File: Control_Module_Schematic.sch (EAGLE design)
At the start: 29 parts, among them U2 ATMEGA328P_TQFP

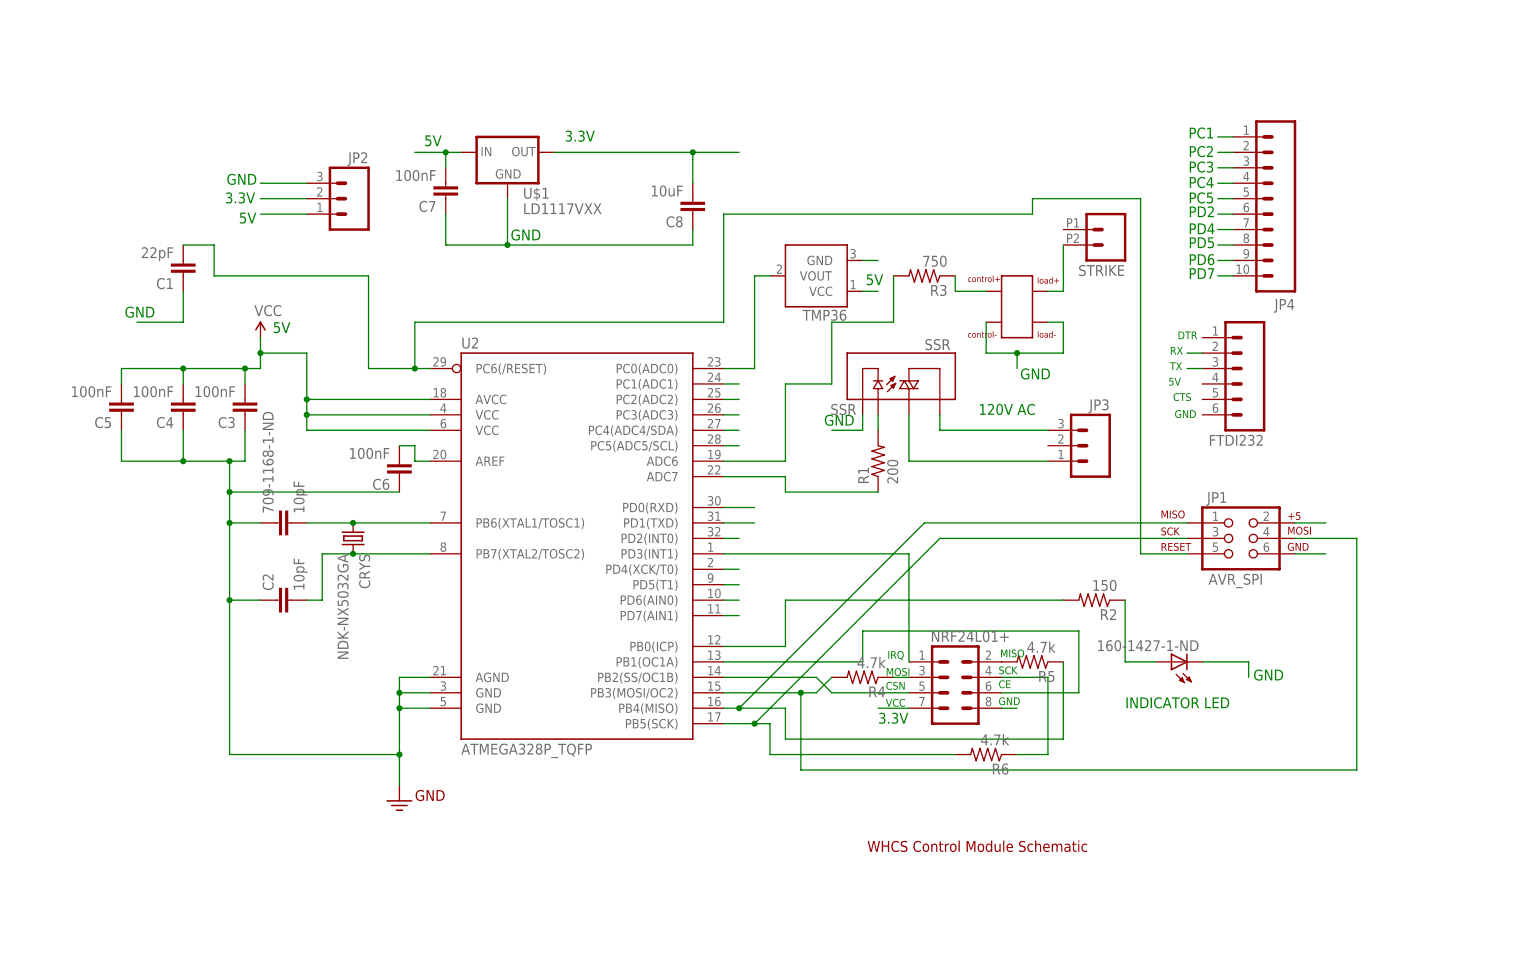
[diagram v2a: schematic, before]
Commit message: fixed drc fail. Two vias were too close together at the top right of the mcu
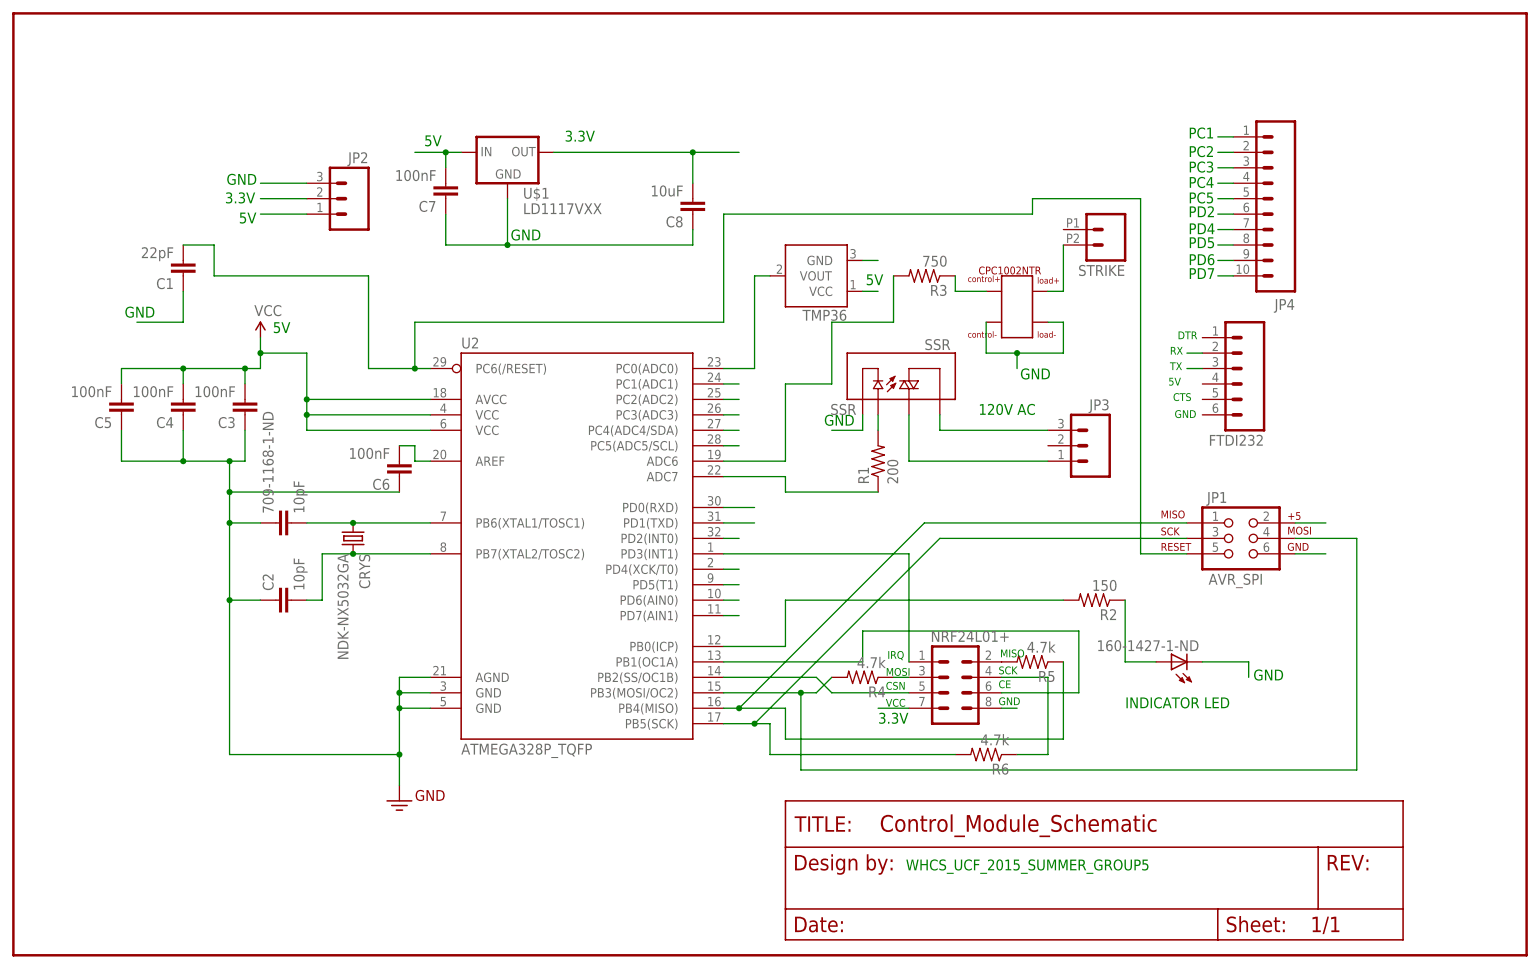
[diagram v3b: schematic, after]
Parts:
- added FRAME1: FRAME-LETTERNO_PACKAGE, WHCS:FRAME-LETTERNO_PACKAGE
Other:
- note added: "WHCS_UCF_2015_SUMMER_GROUP5"
- note removed: "WHCS Control Module Schematic"
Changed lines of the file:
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@@
 <part name="JP3" library="SparkFun-Connectors" deviceset="M03" device="-SCREW-5MM"/>
 <part name="JP4" library="SparkFun-Connectors" deviceset="M10" device="LOCK_LONGPADS"/>
+<part name="FRAME1" library="WHCS" deviceset="FRAME-LETTER" device="NO_PACKAGE"/>
 </parts>
 <sheets>
@@
 <text x="20.32" y="-33.02" size="1.778" layer="91">3.3V</text>
 <text x="60.96" y="-30.48" size="1.778" layer="91">INDICATOR LED</text>
-<text x="18.542" y="-54.102" size="1.778" layer="94">WHCS Control Module Schematic</text>
 <text x="-87.122" y="52.578" size="1.778" layer="91">3.3V</text>
 <text x="43.688" y="23.622" size="1.778" layer="91">GND</text>
@@
 <text x="71.374" y="42.418" size="1.778" layer="91">PD6</text>
 <text x="71.374" y="40.132" size="1.778" layer="91">PD7</text>
+<text x="24.892" y="-57.15" size="1.778" layer="91">WHCS_UCF_2015_SUMMER_GROUP5</text>
 </plain>
 <instances>
@@
 <instance part="JP3" gate="G$1" x="55.88" y="12.7" rot="MR0"/>
 <instance part="JP4" gate="G$1" x="88.9" y="45.72" rot="R180"/>
+<instance part="FRAME1" gate="G$1" x="-121.92" y="-71.12"/>
+<instance part="FRAME1" gate="V" x="5.08" y="-68.58"/>
 </instances>
 <busses>

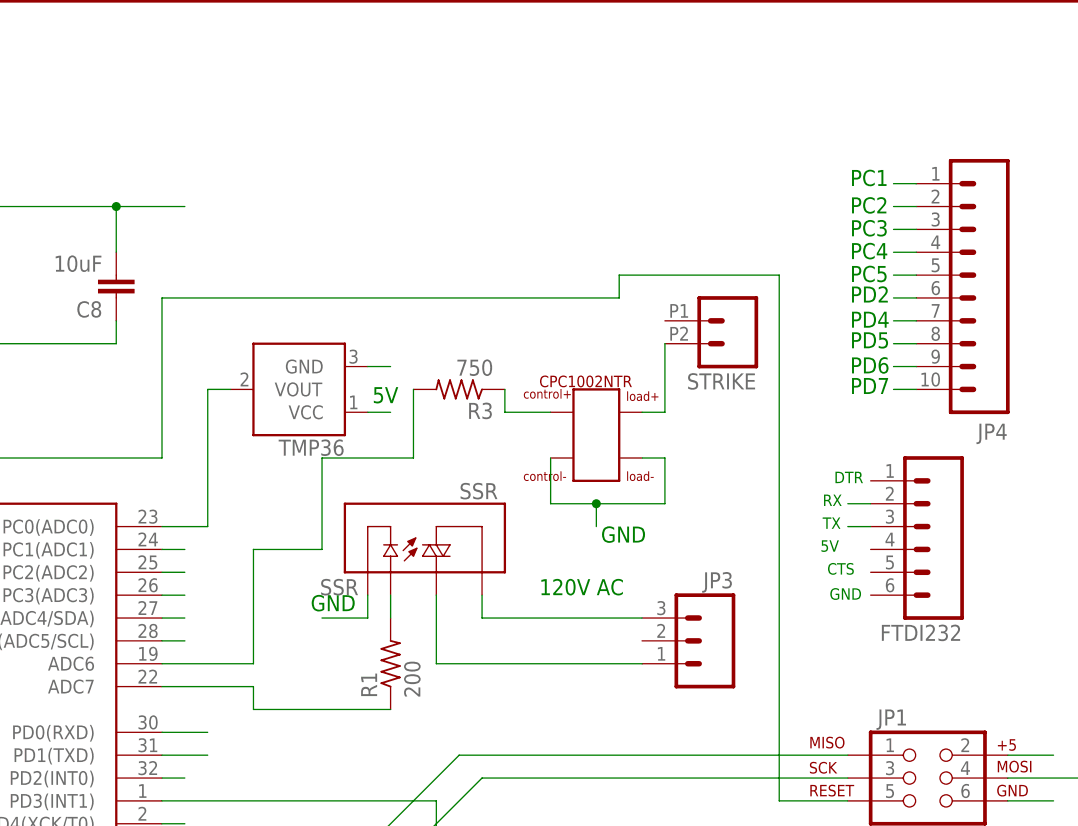
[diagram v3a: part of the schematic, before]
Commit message: Changed the pin that controls the door strike
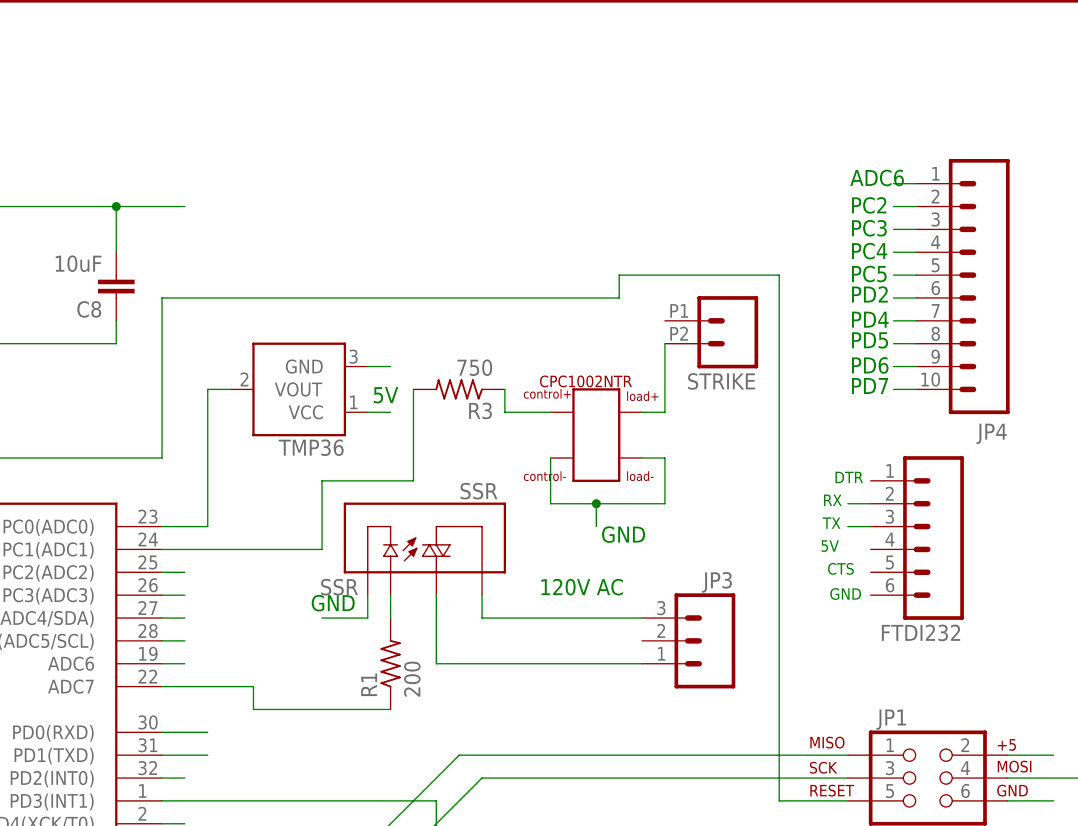
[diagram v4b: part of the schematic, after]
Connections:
- removed net N$19: R3.2, U2.ADC6
- removed net PC1: JP4.1, U2.PC1(ADC1)
- new net ADC6: JP4.1, U2.ADC6
- new net N$12: R3.2, U2.PC1(ADC1)
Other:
- note added: "ADC6"
- note removed: "PC1"
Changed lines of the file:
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@@
 <text x="-31.242" y="62.738" size="1.778" layer="91">3.3V</text>
 <text x="-54.356" y="61.976" size="1.778" layer="91">5V</text>
-<text x="71.374" y="63.246" size="1.778" layer="91">PC1</text>
+<text x="71.374" y="63.246" size="1.778" layer="91">ADC6</text>
 <text x="71.374" y="60.198" size="1.778" layer="91">PC2</text>
 <text x="71.374" y="57.658" size="1.778" layer="91">PC3</text>
@@
 </segment>
 </net>
-<net name="N$19" class="0">
-<segment>
-<wire x1="22.86" y1="33.02" x2="12.7" y2="33.02" width="0.1524" layer="91"/>
-<wire x1="12.7" y1="33.02" x2="12.7" y2="22.86" width="0.1524" layer="91"/>
-<wire x1="12.7" y1="22.86" x2="5.08" y2="22.86" width="0.1524" layer="91"/>
-<wire x1="5.08" y1="22.86" x2="5.08" y2="10.16" width="0.1524" layer="91"/>
-<wire x1="5.08" y1="10.16" x2="-5.08" y2="10.16" width="0.1524" layer="91"/>
-<wire x1="22.86" y1="33.02" x2="22.86" y2="40.64" width="0.1524" layer="91"/>
-<pinref part="R3" gate="G$1" pin="2"/>
-<pinref part="U2" gate="U$1" pin="ADC6"/>
-</segment>
-</net>
 <net name="N$13" class="0">
 <segment>
@@
 </segment>
 </net>
-<net name="PC1" class="0">
+<net name="PC2" class="0">
+<segment>
+<pinref part="JP4" gate="G$1" pin="2"/>
+<wire x1="78.74" y1="60.96" x2="76.2" y2="60.96" width="0.1524" layer="91"/>
+</segment>
+<segment>
+<pinref part="U2" gate="U$1" pin="PC2(ADC2)"/>
+<wire x1="-5.08" y1="20.32" x2="-2.54" y2="20.32" width="0.1524" layer="91"/>
+</segment>
+</net>
+<net name="PC3" class="0">
+<segment>
+<pinref part="JP4" gate="G$1" pin="3"/>
+<wire x1="78.74" y1="58.42" x2="76.2" y2="58.42" width="0.1524" layer="91"/>
+</segment>
+<segment>
+<pinref part="U2" gate="U$1" pin="PC3(ADC3)"/>
+<wire x1="-5.08" y1="17.78" x2="-2.54" y2="17.78" width="0.1524" layer="91"/>
+</segment>
+</net>
+<net name="PC4" class="0">
+<segment>
+<pinref part="JP4" gate="G$1" pin="4"/>
+<wire x1="78.74" y1="55.88" x2="76.2" y2="55.88" width="0.1524" layer="91"/>
+</segment>
+<segment>
+<pinref part="U2" gate="U$1" pin="PC4(ADC4/SDA)"/>
+<wire x1="-5.08" y1="15.24" x2="-2.54" y2="15.24" width="0.1524" layer="91"/>
+</segment>
+</net>
+<net name="PC5" class="0">
+<segment>
+<pinref part="JP4" gate="G$1" pin="5"/>
+<wire x1="78.74" y1="53.34" x2="76.2" y2="53.34" width="0.1524" layer="91"/>
+</segment>
+<segment>
+<pinref part="U2" gate="U$1" pin="PC5(ADC5/SCL)"/>
+<wire x1="-5.08" y1="12.7" x2="-2.54" y2="12.7" width="0.1524" layer="91"/>
+</segment>
+</net>
+<net name="PD2" class="0">
+<segment>
+<pinref part="JP4" gate="G$1" pin="6"/>
+<wire x1="78.74" y1="50.8" x2="76.2" y2="50.8" width="0.1524" layer="91"/>
+</segment>
+<segment>
+<pinref part="U2" gate="U$1" pin="PD2(INT0)"/>
+<wire x1="-5.08" y1="-2.54" x2="-2.54" y2="-2.54" width="0.1524" layer="91"/>
+</segment>
+</net>
+<net name="PD4" class="0">
+<segment>
+<pinref part="JP4" gate="G$1" pin="7"/>
+<wire x1="78.74" y1="48.26" x2="76.2" y2="48.26" width="0.1524" layer="91"/>
+</segment>
+<segment>
+<pinref part="U2" gate="U$1" pin="PD4(XCK/T0)"/>
+<wire x1="-5.08" y1="-7.62" x2="-2.54" y2="-7.62" width="0.1524" layer="91"/>
+</segment>
+</net>
+<net name="PD5" class="0">
+<segment>
+<pinref part="JP4" gate="G$1" pin="8"/>
+<wire x1="78.74" y1="45.72" x2="76.2" y2="45.72" width="0.1524" layer="91"/>
+</segment>
+<segment>
+<pinref part="U2" gate="U$1" pin="PD5(T1)"/>
+<wire x1="-5.08" y1="-10.16" x2="-2.54" y2="-10.16" width="0.1524" layer="91"/>
+</segment>
+</net>
+<net name="PD6" class="0">
+<segment>
+<pinref part="JP4" gate="G$1" pin="9"/>
+<wire x1="78.74" y1="43.18" x2="76.2" y2="43.18" width="0.1524" layer="91"/>
+</segment>
+<segment>
+<pinref part="U2" gate="U$1" pin="PD6(AIN0)"/>
+<wire x1="-5.08" y1="-12.7" x2="-2.54" y2="-12.7" width="0.1524" layer="91"/>
+</segment>
+</net>
+<net name="PD7" class="0">
+<segment>
+<pinref part="JP4" gate="G$1" pin="10"/>
+<wire x1="78.74" y1="40.64" x2="76.2" y2="40.64" width="0.1524" layer="91"/>
+</segment>
+<segment>
+<pinref part="U2" gate="U$1" pin="PD7(AIN1)"/>
+<wire x1="-5.08" y1="-15.24" x2="-2.54" y2="-15.24" width="0.1524" layer="91"/>
+</segment>
+</net>
+<net name="N$12" class="0">
+<segment>
+<pinref part="U2" gate="U$1" pin="PC1(ADC1)"/>
+<wire x1="-5.08" y1="22.86" x2="12.7" y2="22.86" width="0.1524" layer="91"/>
+<wire x1="12.7" y1="22.86" x2="12.7" y2="30.48" width="0.1524" layer="91"/>
+<wire x1="12.7" y1="30.48" x2="22.86" y2="30.48" width="0.1524" layer="91"/>
+<pinref part="R3" gate="G$1" pin="2"/>
+<wire x1="22.86" y1="30.48" x2="22.86" y2="40.64" width="0.1524" layer="91"/>
+</segment>
+</net>
+<net name="ADC6" class="0">
 <segment>
 <pinref part="JP4" gate="G$1" pin="1"/>
@@
 </segment>
 <segment>
-<pinref part="U2" gate="U$1" pin="PC1(ADC1)"/>
-<wire x1="-5.08" y1="22.86" x2="-2.54" y2="22.86" width="0.1524" layer="91"/>
-</segment>
-</net>
-<net name="PC2" class="0">
-<segment>
-<pinref part="JP4" gate="G$1" pin="2"/>
-<wire x1="78.74" y1="60.96" x2="76.2" y2="60.96" width="0.1524" layer="91"/>
-</segment>
-<segment>
-<pinref part="U2" gate="U$1" pin="PC2(ADC2)"/>
-<wire x1="-5.08" y1="20.32" x2="-2.54" y2="20.32" width="0.1524" layer="91"/>
-</segment>
-</net>
-<net name="PC3" class="0">
-<segment>
-<pinref part="JP4" gate="G$1" pin="3"/>
-<wire x1="78.74" y1="58.42" x2="76.2" y2="58.42" width="0.1524" layer="91"/>
-</segment>
-<segment>
-<pinref part="U2" gate="U$1" pin="PC3(ADC3)"/>
-<wire x1="-5.08" y1="17.78" x2="-2.54" y2="17.78" width="0.1524" layer="91"/>
-</segment>
-</net>
-<net name="PC4" class="0">
-<segment>
-<pinref part="JP4" gate="G$1" pin="4"/>
-<wire x1="78.74" y1="55.88" x2="76.2" y2="55.88" width="0.1524" layer="91"/>
-</segment>
-<segment>
-<pinref part="U2" gate="U$1" pin="PC4(ADC4/SDA)"/>
-<wire x1="-5.08" y1="15.24" x2="-2.54" y2="15.24" width="0.1524" layer="91"/>
-</segment>
-</net>
-<net name="PC5" class="0">
-<segment>
-<pinref part="JP4" gate="G$1" pin="5"/>
-<wire x1="78.74" y1="53.34" x2="76.2" y2="53.34" width="0.1524" layer="91"/>
-</segment>
-<segment>
-<pinref part="U2" gate="U$1" pin="PC5(ADC5/SCL)"/>
-<wire x1="-5.08" y1="12.7" x2="-2.54" y2="12.7" width="0.1524" layer="91"/>
-</segment>
-</net>
-<net name="PD2" class="0">
-<segment>
-<pinref part="JP4" gate="G$1" pin="6"/>
-<wire x1="78.74" y1="50.8" x2="76.2" y2="50.8" width="0.1524" layer="91"/>
-</segment>
-<segment>
-<pinref part="U2" gate="U$1" pin="PD2(INT0)"/>
-<wire x1="-5.08" y1="-2.54" x2="-2.54" y2="-2.54" width="0.1524" layer="91"/>
-</segment>
-</net>
-<net name="PD4" class="0">
-<segment>
-<pinref part="JP4" gate="G$1" pin="7"/>
-<wire x1="78.74" y1="48.26" x2="76.2" y2="48.26" width="0.1524" layer="91"/>
-</segment>
-<segment>
-<pinref part="U2" gate="U$1" pin="PD4(XCK/T0)"/>
-<wire x1="-5.08" y1="-7.62" x2="-2.54" y2="-7.62" width="0.1524" layer="91"/>
-</segment>
-</net>
-<net name="PD5" class="0">
-<segment>
-<pinref part="JP4" gate="G$1" pin="8"/>
-<wire x1="78.74" y1="45.72" x2="76.2" y2="45.72" width="0.1524" layer="91"/>
-</segment>
-<segment>
-<pinref part="U2" gate="U$1" pin="PD5(T1)"/>
-<wire x1="-5.08" y1="-10.16" x2="-2.54" y2="-10.16" width="0.1524" layer="91"/>
-</segment>
-</net>
-<net name="PD6" class="0">
-<segment>
-<pinref part="JP4" gate="G$1" pin="9"/>
-<wire x1="78.74" y1="43.18" x2="76.2" y2="43.18" width="0.1524" layer="91"/>
-</segment>
-<segment>
-<pinref part="U2" gate="U$1" pin="PD6(AIN0)"/>
-<wire x1="-5.08" y1="-12.7" x2="-2.54" y2="-12.7" width="0.1524" layer="91"/>
-</segment>
-</net>
-<net name="PD7" class="0">
-<segment>
-<pinref part="JP4" gate="G$1" pin="10"/>
-<wire x1="78.74" y1="40.64" x2="76.2" y2="40.64" width="0.1524" layer="91"/>
-</segment>
-<segment>
-<pinref part="U2" gate="U$1" pin="PD7(AIN1)"/>
-<wire x1="-5.08" y1="-15.24" x2="-2.54" y2="-15.24" width="0.1524" layer="91"/>
-</segment>
-</net>
+<pinref part="U2" gate="U$1" pin="ADC6"/>
+<wire x1="-5.08" y1="10.16" x2="-2.54" y2="10.16" width="0.1524" layer="91"/>
+</segment>
+</net>

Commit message: Connected the FTDI232 UART chip's GND to GND
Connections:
- net GND: now also FTDI232.6
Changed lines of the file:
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@@
 <wire x1="-10.16" y1="45.72" x2="-40.64" y2="45.72" width="0.1524" layer="91"/>
+</segment>
+<segment>
+<pinref part="FTDI232" gate="G$1" pin="6"/>
+<wire x1="73.66" y1="17.78" x2="73.66" y2="15.24" width="0.1524" layer="91"/>
 </segment>
 </net>

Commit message: AC solid state relay pin change
The AC SSR is now controlled by pc2 from the atmega328. The previous pin
used to control it ADC7 was not capable of producing output and it has
been rerouted to the breakout header.
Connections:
- removed net PC2: JP4.2, U2.PC2(ADC2)
- new net ADC7: JP4.2, U2.ADC7
- net N$9: now also U2.PC2(ADC2); no longer U2.ADC7
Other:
- note added: "AD7"
- note removed: "PC2"
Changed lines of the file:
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@@
 <text x="-54.356" y="61.976" size="1.778" layer="91">5V</text>
 <text x="71.374" y="63.246" size="1.778" layer="91">ADC6</text>
-<text x="71.374" y="60.198" size="1.778" layer="91">PC2</text>
+<text x="71.374" y="60.198" size="1.778" layer="91">AD7</text>
 <text x="71.374" y="57.658" size="1.778" layer="91">PC3</text>
 <text x="71.374" y="55.118" size="1.778" layer="91">PC4</text>
@@
 </segment>
 </net>
-<net name="N$9" class="0">
-<segment>
-<wire x1="-5.08" y1="7.62" x2="5.08" y2="7.62" width="0.1524" layer="91"/>
-<wire x1="5.08" y1="7.62" x2="5.08" y2="5.08" width="0.1524" layer="91"/>
-<pinref part="R1" gate="G$1" pin="1"/>
-<wire x1="5.08" y1="5.08" x2="20.32" y2="5.08" width="0.1524" layer="91"/>
-<pinref part="U2" gate="U$1" pin="ADC7"/>
-</segment>
-</net>
 <net name="N$11" class="0">
 <segment>
@@
 </segment>
 </net>
-<net name="PC2" class="0">
-<segment>
-<pinref part="JP4" gate="G$1" pin="2"/>
-<wire x1="78.74" y1="60.96" x2="76.2" y2="60.96" width="0.1524" layer="91"/>
-</segment>
-<segment>
-<pinref part="U2" gate="U$1" pin="PC2(ADC2)"/>
-<wire x1="-5.08" y1="20.32" x2="-2.54" y2="20.32" width="0.1524" layer="91"/>
-</segment>
-</net>
 <net name="PC3" class="0">
 <segment>
@@
 </segment>
 </net>
+<net name="N$9" class="0">
+<segment>
+<pinref part="U2" gate="U$1" pin="PC2(ADC2)"/>
+<wire x1="-5.08" y1="20.32" x2="10.16" y2="20.32" width="0.1524" layer="91"/>
+<wire x1="10.16" y1="20.32" x2="10.16" y2="5.08" width="0.1524" layer="91"/>
+<pinref part="R1" gate="G$1" pin="1"/>
+<wire x1="10.16" y1="5.08" x2="20.32" y2="5.08" width="0.1524" layer="91"/>
+</segment>
+</net>
+<net name="ADC7" class="0">
+<segment>
+<pinref part="U2" gate="U$1" pin="ADC7"/>
+<wire x1="-5.08" y1="7.62" x2="-2.54" y2="7.62" width="0.1524" layer="91"/>
+</segment>
+<segment>
+<pinref part="JP4" gate="G$1" pin="2"/>
+<wire x1="78.74" y1="60.96" x2="76.2" y2="60.96" width="0.1524" layer="91"/>
+</segment>
+</net>
